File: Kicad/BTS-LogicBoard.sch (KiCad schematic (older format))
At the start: 52 parts, among them J1 Conn_01x06, J2 Conn_01x04, J3 Conn_01x02, Q1 BC817, Q2 BC807, Q3 BC817, Q4 BC807, Q5 BC817, Q6 BC817, SW1 SW_DPDT_x2, SW2 SW_DPDT_x2, U1 NCS2252SN2T1G, U2 NE555D, U3 NCS2252SN2T1G

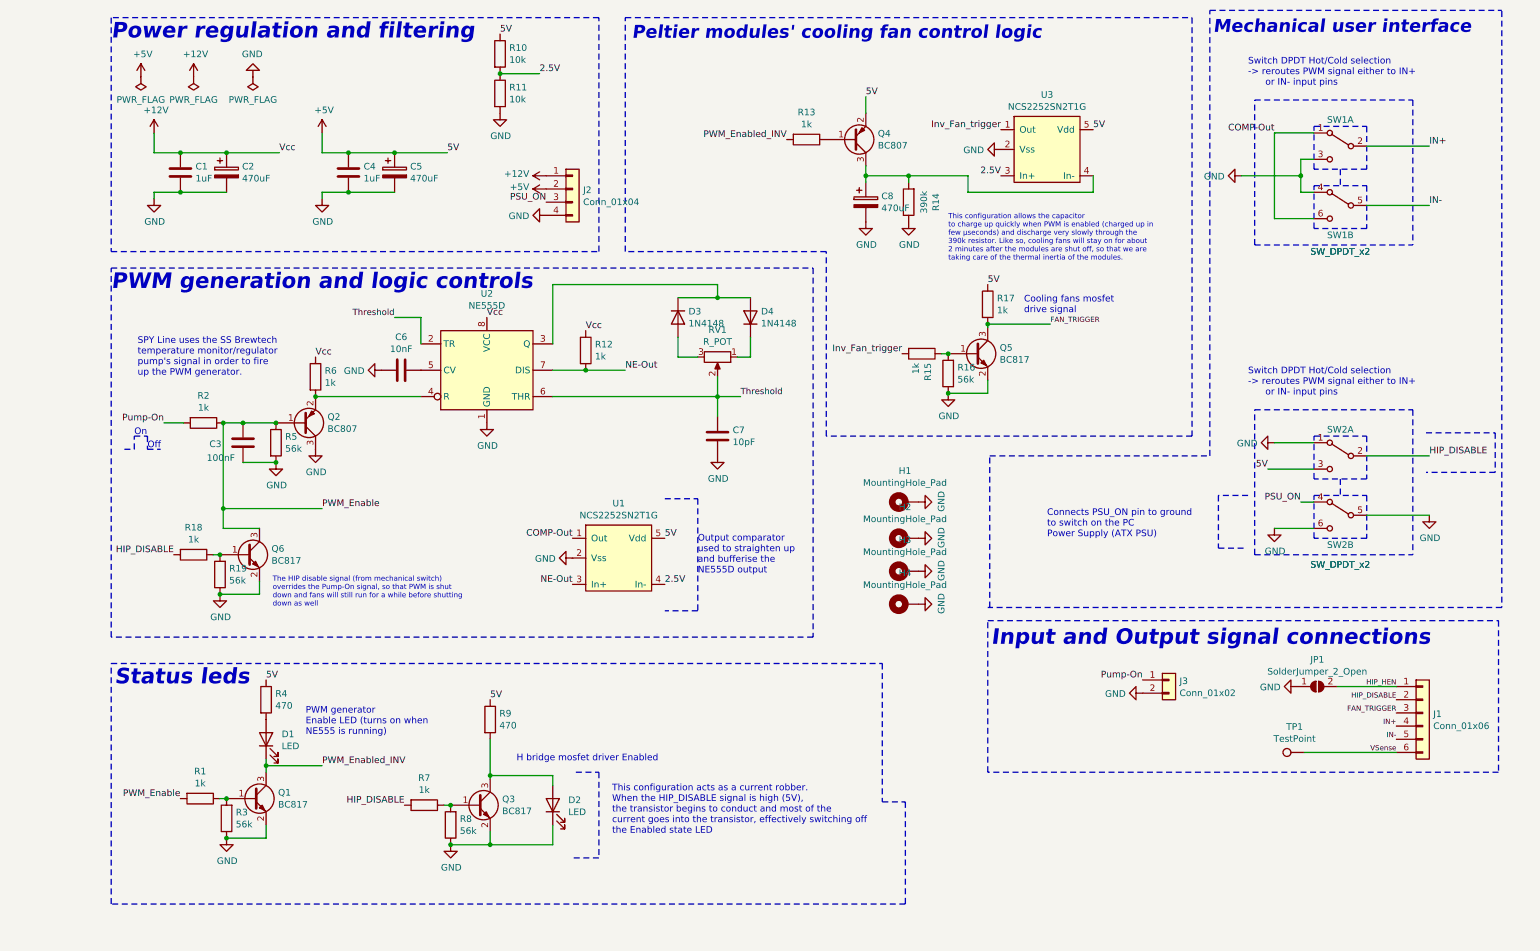
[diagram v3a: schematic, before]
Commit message: Updated board with optocoupler
Signed-off-by: bebenlebricolo <benoittarrade@hotmail.fr>
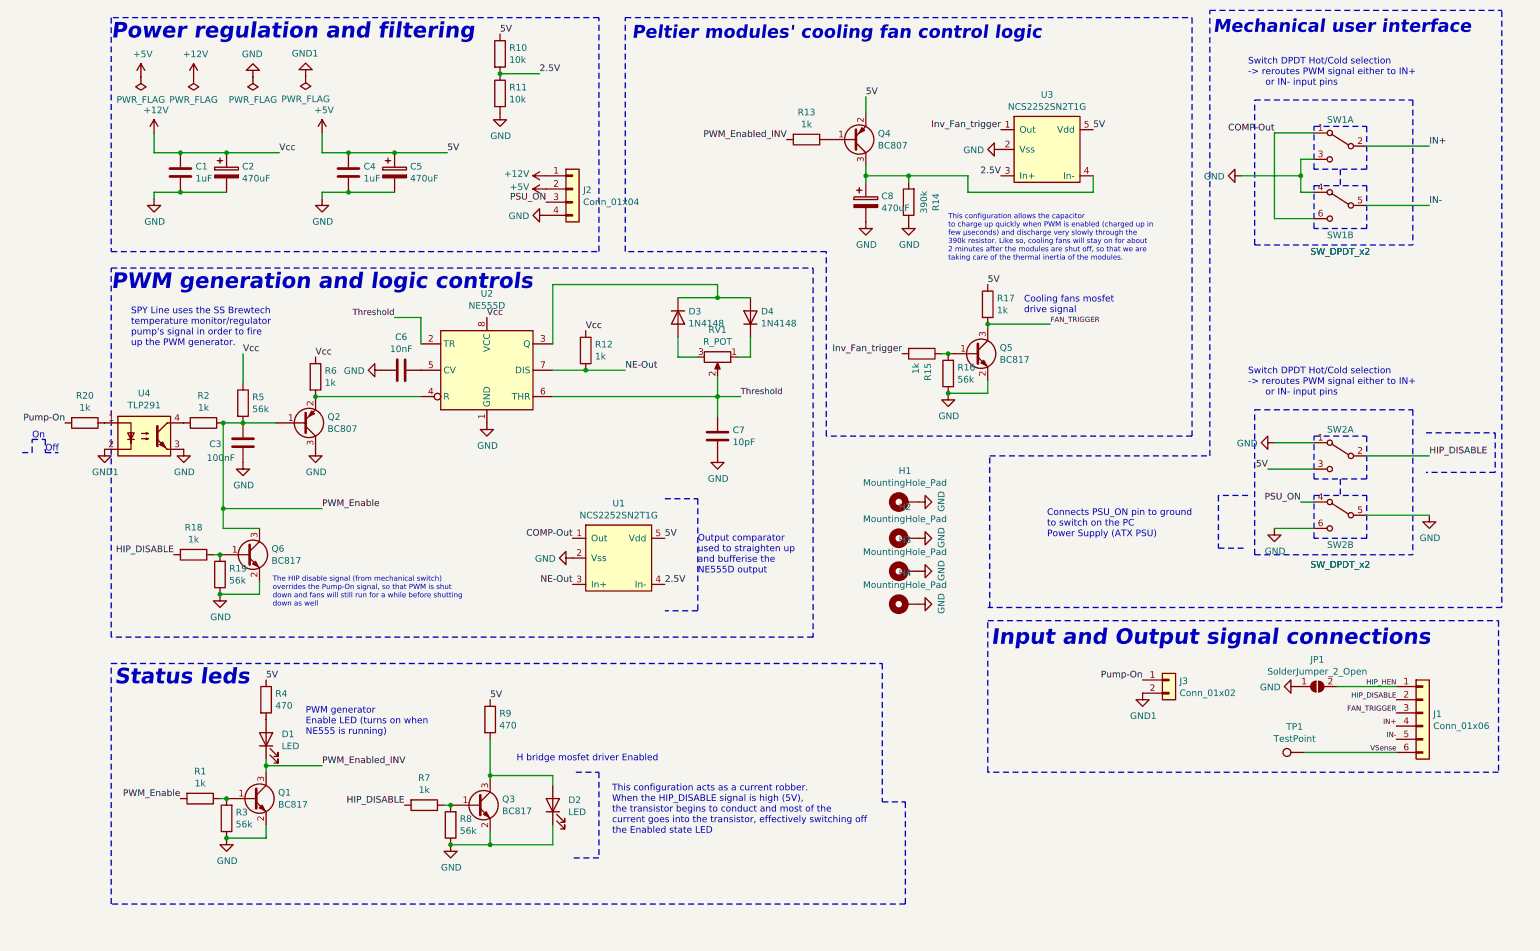
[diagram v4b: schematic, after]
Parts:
- added R20: 1k, Resistor_SMD:R_1206_3216Metric_Pad1.30x1.75mm_HandSolder, symbol Device:R
- added U4: TLP291, Package_SO:SOIC-4_4.55x2.6mm_P1.27mm, symbol Isolator:TLP291
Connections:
- net +12V: now also R5.1
- net GND: now also U4.3; no longer J3.2 (Pin_2), R5.2
- net PWM_Enable: now also R5.2; no longer R5.1
- net Pump-On: now also R20.2; no longer R2.2
- new net: R2.2, U4.4
- new net: R20.1, U4.1
- new net GND1: J3.2 (Pin_2), U4.2
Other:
- moved on the sheet: R5
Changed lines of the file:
@@
-$EndComp
-$Comp
-L Device:R R5
-U 1 1 613CFCC9
-P 1875 3800
-F 0 "R5" H 1945 3846 50  0000 L CNN
-F 1 "56k" H 1945 3755 50  0000 L CNN
-F 2 "Resistor_SMD:R_1206_3216Metric_Pad1.30x1.75mm_HandSolder" V 1805 3800 50  0001 C CNN
-F 3 "~" H 1875 3800 50  0001 C CNN
-	1    1875 3800
-	1    0    0    -1
-$EndComp
-$Comp
-L power:GND #PWR0109
-U 1 1 613D002F
-P 1875 3950
-F 0 "#PWR0109" H 1875 3700 50  0001 C CNN
-F 1 "GND" H 1880 3777 50  0000 C CNN
-F 2 "" H 1875 3950 50  0001 C CNN
-F 3 "" H 1875 3950 50  0001 C CNN
-	1    1875 3950
-	1    0    0    -1
 $EndComp
 $Comp
@@
 Wire Wire Line
 	1475 3650 1625 3650
-Connection ~ 1875 3650
 Connection ~ 1625 3650
 Wire Wire Line
 	1625 3650 1875 3650
-Wire Wire Line
-	1625 3950 1875 3950
-Connection ~ 1875 3950
-Wire Wire Line
-	1175 3650 1025 3650
-Text Label 1025 3650 2    50   ~ 0
+Text Label 275  3650 2    50   ~ 0
 Pump-On
 $Comp
@@
 Text Notes 2100 6025 0    50   ~ 0
 PWM generator \nEnable LED (turns on when \nNE555 is running)
-Text Notes 825  3300 0    50   ~ 0
+Text Notes 775  3075 0    50   ~ 0
 SPY Line uses the SS Brewtech \ntemperature monitor/regulator\npump's signal in order to fire\nup the PWM generator.
 Text Label 3575 700  0    50   ~ 0
@@
 	1    0    0    -1
 $EndComp
-$Comp
-L power:GND #PWR04
-U 1 1 6162B46D
-P 8450 5700
-F 0 "#PWR04" H 8450 5450 50  0001 C CNN
-F 1 "GND" V 8455 5572 50  0000 R CNN
-F 2 "" H 8450 5700 50  0001 C CNN
-F 3 "" H 8450 5700 50  0001 C CNN
-	1    8450 5700
-	0    1    1    0
-$EndComp
 Wire Notes Line
 	7275 5150 11150 5150
@@
 Pump-On
 Wire Notes Line
-	725  3850 800  3850
-Wire Notes Line
-	800  3850 800  3750
-Wire Notes Line
-	800  3750 900  3750
-Wire Notes Line
-	900  3750 900  3850
-Wire Notes Line
-	900  3850 1000 3850
-Text Notes 800  3750 0    50   ~ 0
+	-50  3875 25   3875
+Wire Notes Line
+	25   3875 25   3775
+Wire Notes Line
+	25   3775 125  3775
+Wire Notes Line
+	125  3775 125  3875
+Wire Notes Line
+	125  3875 225  3875
+Text Notes 25   3775 0    50   ~ 0
 On
-Text Notes 900  3850 0    50   ~ 0
+Text Notes 125  3875 0    50   ~ 0
 Off
 $Comp
@@
 Text Label 7275 2600 0    50   ~ 0
 5V
+$Comp
+L Isolator:TLP291 U4
+U 1 1 6156BE0A
+P 875 3750
+F 0 "U4" H 875 4075 50  0000 C CNN
+F 1 "TLP291" H 875 3984 50  0000 C CNN
+F 2 "Package_SO:SOIC-4_4.55x2.6mm_P1.27mm" H 675 3550 50  0001 L CIN
+F 3 "https://toshiba.semicon-storage.com/info/docget.jsp?did=12884&prodName=TLP291" H 875 3750 50  0001 L CNN
+	1    875  3750
+	1    0    0    -1
+$EndComp
+$Comp
+L Device:R R20
+U 1 1 615751E4
+P 425 3650
+F 0 "R20" V 218 3650 50  0000 C CNN
+F 1 "1k" V 309 3650 50  0000 C CNN
+F 2 "Resistor_SMD:R_1206_3216Metric_Pad1.30x1.75mm_HandSolder" V 355 3650 50  0001 C CNN
+F 3 "~" H 425 3650 50  0001 C CNN
+	1    425  3650
+	0    1    1    0
+$EndComp
+$Comp
+L power:GND1 #PWR0109
+U 1 1 6157887E
+P 575 3850
+F 0 "#PWR0109" H 575 3600 50  0001 C CNN
+F 1 "GND1" H 580 3677 50  0000 C CNN
+F 2 "" H 575 3850 50  0001 C CNN
+F 3 "" H 575 3850 50  0001 C CNN
+	1    575  3850
+	1    0    0    -1
+$EndComp
+$Comp
+L power:GND1 #PWR0121
+U 1 1 61578E5E
+P 2100 1020
+F 0 "#PWR0121" H 2100 770 50  0001 C CNN
+F 1 "GND1" H 2105 847 50  0000 C CNN
+F 2 "" H 2100 1020 50  0001 C CNN
+F 3 "" H 2100 1020 50  0001 C CNN
+	1    2100 1020
+	-1   0    0    1
+$EndComp
+$Comp
+L power:PWR_FLAG #FLG0104
+U 1 1 61583121
+P 2100 1020
+F 0 "#FLG0104" H 2100 1095 50  0001 C CNN
+F 1 "PWR_FLAG" H 2100 1193 50  0000 C CNN
+F 2 "" H 2100 1020 50  0001 C CNN
+F 3 "~" H 2100 1020 50  0001 C CNN
+	1    2100 1020
+	-1   0    0    1
+$EndComp
+$Comp
+L power:GND #PWR0123
+U 1 1 615A56AF
+P 1175 3850
+F 0 "#PWR0123" H 1175 3600 50  0001 C CNN
+F 1 "GND" H 1180 3677 50  0000 C CNN
+F 2 "" H 1175 3850 50  0001 C CNN
+F 3 "" H 1175 3850 50  0001 C CNN
+	1    1175 3850
+	1    0    0    -1
+$EndComp
+$Comp
+L Device:R R5
+U 1 1 613CFCC9
+P 1625 3500
+F 0 "R5" H 1695 3546 50  0000 L CNN
+F 1 "56k" H 1695 3455 50  0000 L CNN
+F 2 "Resistor_SMD:R_1206_3216Metric_Pad1.30x1.75mm_HandSolder" V 1555 3500 50  0001 C CNN
+F 3 "~" H 1625 3500 50  0001 C CNN
+	1    1625 3500
+	1    0    0    -1
+$EndComp
+$Comp
+L power:GND #PWR0124
+U 1 1 6162623B
+P 1625 3950
+F 0 "#PWR0124" H 1625 3700 50  0001 C CNN
+F 1 "GND" H 1630 3777 50  0000 C CNN
+F 2 "" H 1625 3950 50  0001 C CNN
+F 3 "" H 1625 3950 50  0001 C CNN
+	1    1625 3950
+	1    0    0    -1
+$EndComp
+Text Label 1625 3125 0    50   ~ 0
+Vcc
+Wire Wire Line
+	1625 3125 1625 3350
+$Comp
+L power:GND1 #PWR?
+U 1 1 61647759
+P 8450 5700
+F 0 "#PWR?" H 8450 5450 50  0001 C CNN
+F 1 "GND1" H 8455 5527 50  0000 C CNN
+F 2 "" H 8450 5700 50  0001 C CNN
+F 3 "" H 8450 5700 50  0001 C CNN
+	1    8450 5700
+	1    0    0    -1
+$EndComp
 $EndSCHEMATC

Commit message: Fixed unatural DPDT switch mapping
Signed-off-by: bebenlebricolo <benoittarrade@hotmail.fr>
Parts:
- SW1, SW2: footprint Connector_PinSocket_2.54mm:PinSocket_2x03_P2.54mm_Vertical -> BTS-LogicBoard:PinSocket_2x03_P2.54mm_Vertical_DPDT_Special
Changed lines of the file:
@@
 F 0 "SW1" H 9950 1750 50  0000 C CNN
 F 1 "SW_DPDT_x2" H 9950 750 50  0000 C CNN
-F 2 "Connector_PinSocket_2.54mm:PinSocket_2x03_P2.54mm_Vertical" H 9950 1550 50  0001 C CNN
+F 2 "BTS-LogicBoard:PinSocket_2x03_P2.54mm_Vertical_DPDT_Special" H 9950 1550 50  0001 C CNN
 F 3 "~" H 9950 1550 50  0001 C CNN
 	1    9950 1550
@@
 F 0 "SW1" H 9950 1775 50  0000 C CNN
 F 1 "SW_DPDT_x2" H 9950 1650 50  0000 C CNN
-F 2 "Connector_PinSocket_2.54mm:PinSocket_2x03_P2.54mm_Vertical" H 9950 2000 50  0001 C CNN
+F 2 "BTS-LogicBoard:PinSocket_2x03_P2.54mm_Vertical_DPDT_Special" H 9950 2000 50  0001 C CNN
 F 3 "~" H 9950 2000 50  0001 C CNN
 	2    9950 2000
@@
 $Comp
 L Switch:SW_DPDT_x2 SW2
-U 1 1 6143E0F8
-P 9950 3900
-F 0 "SW2" H 9950 4100 50  0000 C CNN
-F 1 "SW_DPDT_x2" H 9950 3075 50  0000 C CNN
-F 2 "Connector_PinSocket_2.54mm:PinSocket_2x03_P2.54mm_Vertical" H 9950 3900 50  0001 C CNN
-F 3 "~" H 9950 3900 50  0001 C CNN
-	1    9950 3900
-	-1   0    0    -1
-$EndComp
-$Comp
-L Switch:SW_DPDT_x2 SW2
 U 2 1 6143E0FE
 P 9950 4350
 F 0 "SW2" H 9950 4125 50  0000 C CNN
 F 1 "SW_DPDT_x2" H 9950 3975 50  0000 C CNN
-F 2 "Connector_PinSocket_2.54mm:PinSocket_2x03_P2.54mm_Vertical" H 9950 4350 50  0001 C CNN
+F 2 "BTS-LogicBoard:PinSocket_2x03_P2.54mm_Vertical_DPDT_Special" H 9950 4350 50  0001 C CNN
 F 3 "~" H 9950 4350 50  0001 C CNN
 	2    9950 4350
@@
 	1625 3125 1625 3350
 $Comp
-L power:GND1 #PWR?
+L power:GND1 #PWR0125
 U 1 1 61647759
 P 8450 5700
-F 0 "#PWR?" H 8450 5450 50  0001 C CNN
+F 0 "#PWR0125" H 8450 5450 50  0001 C CNN
 F 1 "GND1" H 8455 5527 50  0000 C CNN
 F 2 "" H 8450 5700 50  0001 C CNN
@@
 	1    0    0    -1
 $EndComp
+$Comp
+L Switch:SW_DPDT_x2 SW2
+U 1 1 6143E0F8
+P 9950 3900
+F 0 "SW2" H 9950 4100 50  0000 C CNN
+F 1 "SW_DPDT_x2" H 9950 3075 50  0000 C CNN
+F 2 "BTS-LogicBoard:PinSocket_2x03_P2.54mm_Vertical_DPDT_Special" H 9950 3900 50  0001 C CNN
+F 3 "~" H 9950 3900 50  0001 C CNN
+	1    9950 3900
+	-1   0    0    -1
+$EndComp
 $EndSCHEMATC

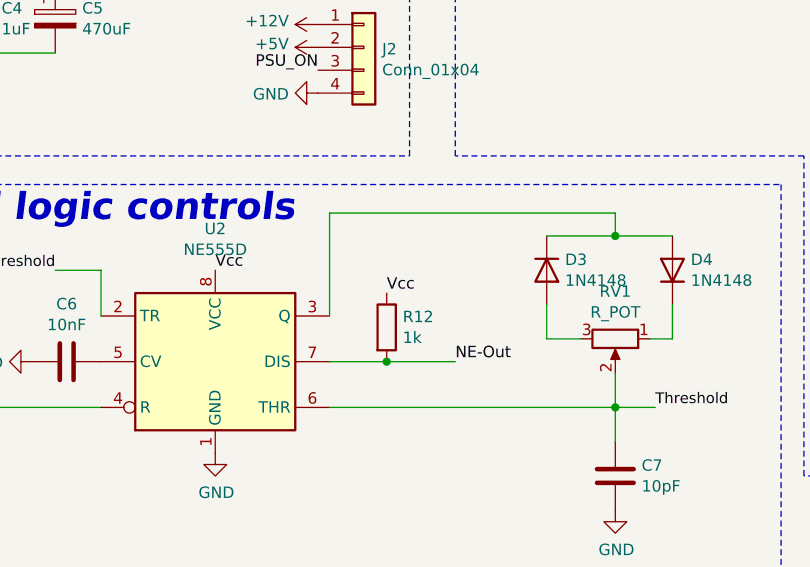
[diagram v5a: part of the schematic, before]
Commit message: Swapped 12Vcc on NE555 outputs and remapped comparators
Signed-off-by: bebenlebricolo <benoittarrade@hotmail.fr>
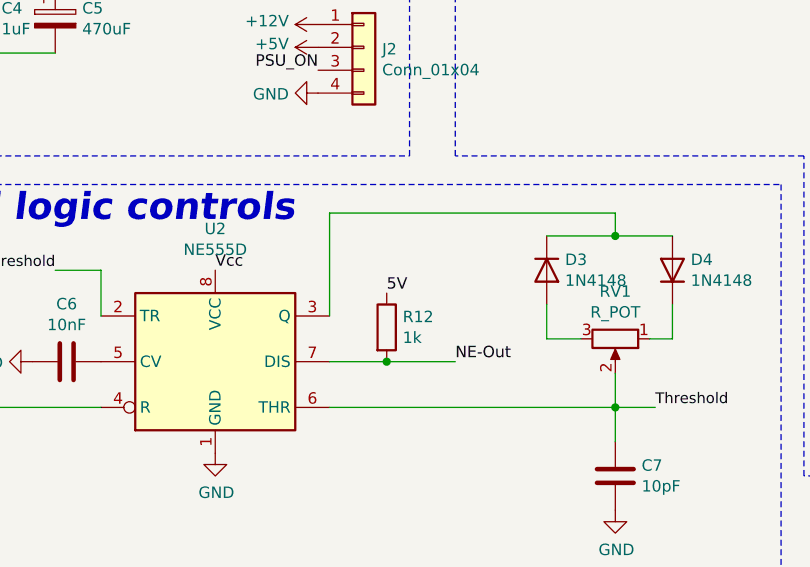
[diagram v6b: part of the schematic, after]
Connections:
- net +12V: no longer R12.1
- net +5V: now also R12.1
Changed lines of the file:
@@
 Wire Wire Line
 	5225 2700 5475 2700
-Text Label 4225 2950 0    50   ~ 0
-Vcc
 $Comp
 L Device:R R12
@@
 	-1   0    0    -1
 $EndComp
+Text Label 4225 2950 0    50   ~ 0
+5V
 $EndSCHEMATC

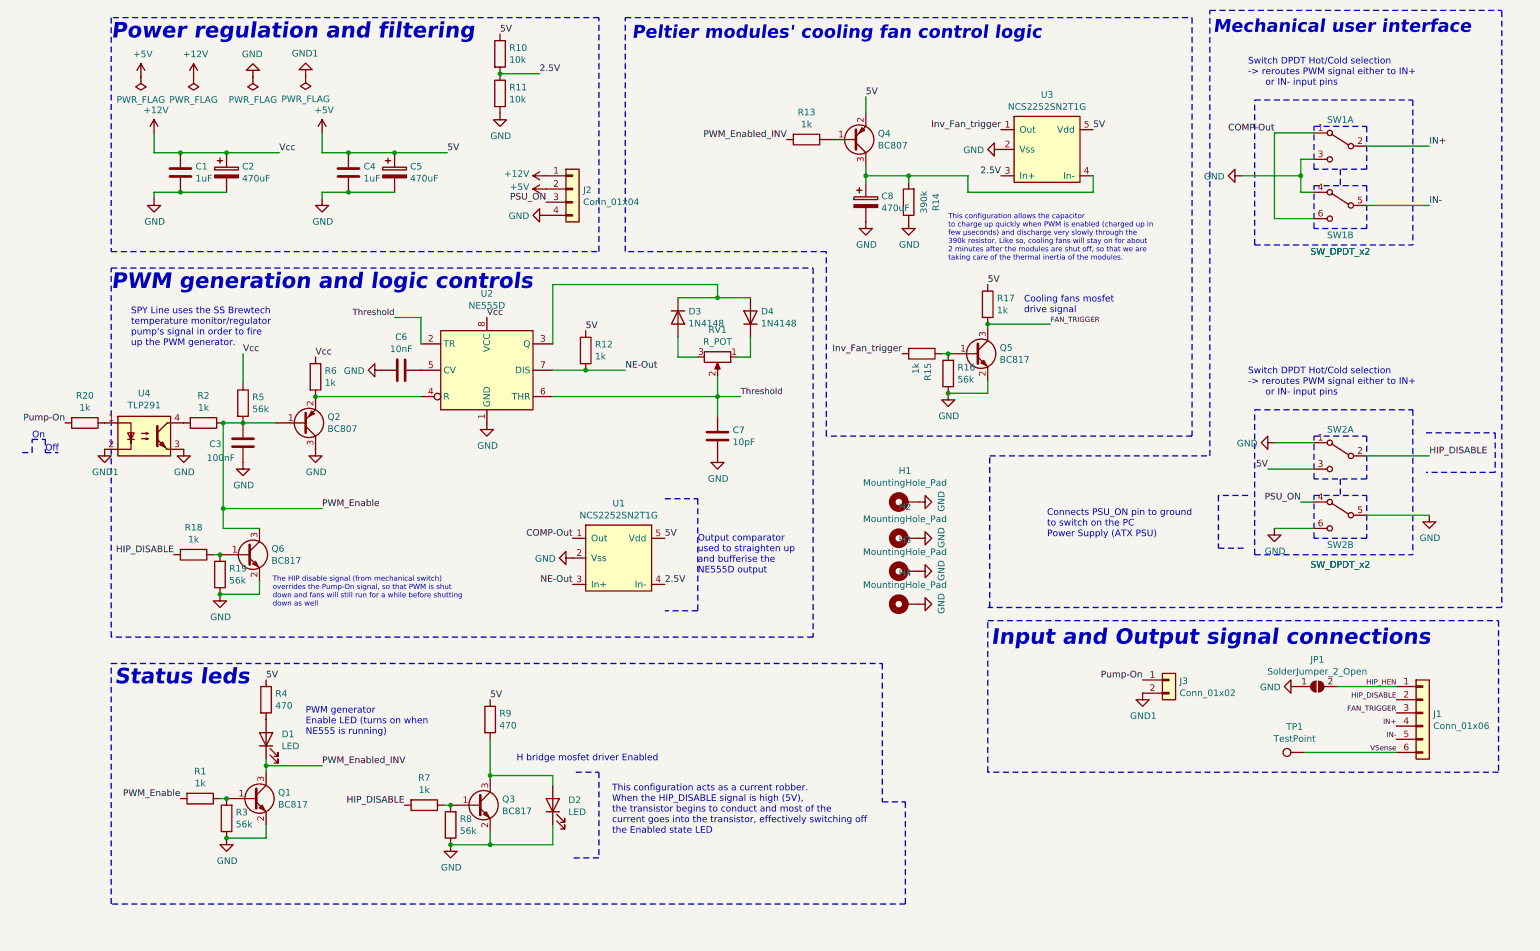
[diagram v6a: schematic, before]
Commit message: Reworking NCS comparators output interface + led logics
Signed-off-by: bebenlebricolo <benoittarrade@hotmail.fr>
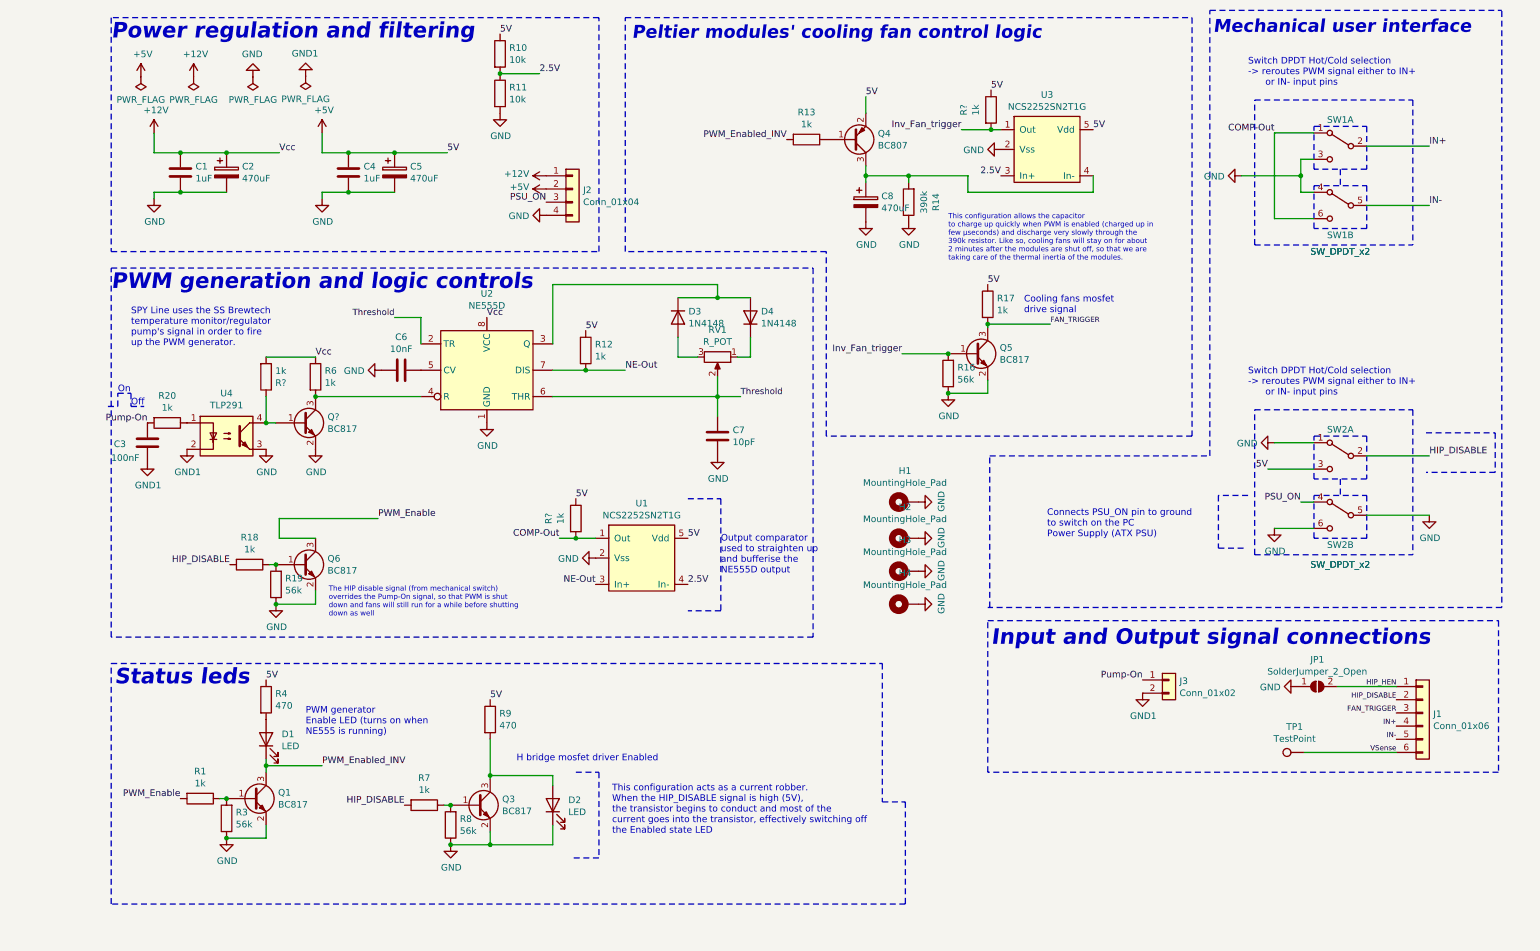
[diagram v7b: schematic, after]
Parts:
- removed Q2: BC807, Package_TO_SOT_SMD:SOT-23, symbol Transistor_BJT:BC807
- removed R15, R2: 1k, Resistor_SMD:R_1206_3216Metric_Pad1.30x1.75mm_HandSolder, symbol Device:R
- removed R5: 56k, Resistor_SMD:R_1206_3216Metric_Pad1.30x1.75mm_HandSolder, symbol Device:R
- added Q?: BC817, Package_TO_SOT_SMD:SOT-23, symbol Transistor_BJT:BC817
- added R? (x3): 1k, Resistor_SMD:R_1206_3216Metric_Pad1.30x1.75mm_HandSolder, symbol Device:R
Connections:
- net +12V: now also R?.2
- net +5V: now also R?.1, R?.1
- net COMP-Out: now also R?.2
- net GND: now also Q?.2 (E); no longer C3.1
- net GND1: now also C3.1
- net Inv_Fan_trigger: now also Q5.1 (B), R16.2, R?.2
- net PWM_Enable: no longer C3.2
- net Pump-On: now also C3.2
- net at R6.2, U2.4 (R): now also Q?.3 (C)
- net at U4.4: now also Q?.1 (B), R?.1
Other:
- moved on the sheet: C3, Q6, R18, R19, R20, U1, U4
